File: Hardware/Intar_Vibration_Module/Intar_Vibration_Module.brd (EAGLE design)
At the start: 17.8 x 25.9 mm, 14 parts, among them J2 GROVE-4P-2.0-3470130P1, M1 MOTORVIBE_COIN_SMD, Q1 MMBT2222A

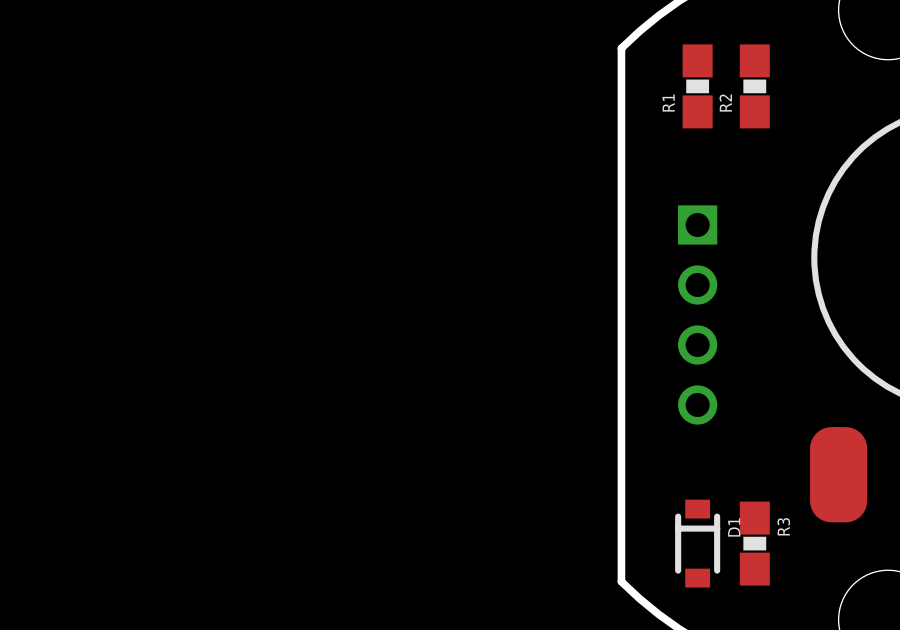
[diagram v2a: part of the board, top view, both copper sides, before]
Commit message: Fixed Grove connectors to be right way (pin 4 should be GND)
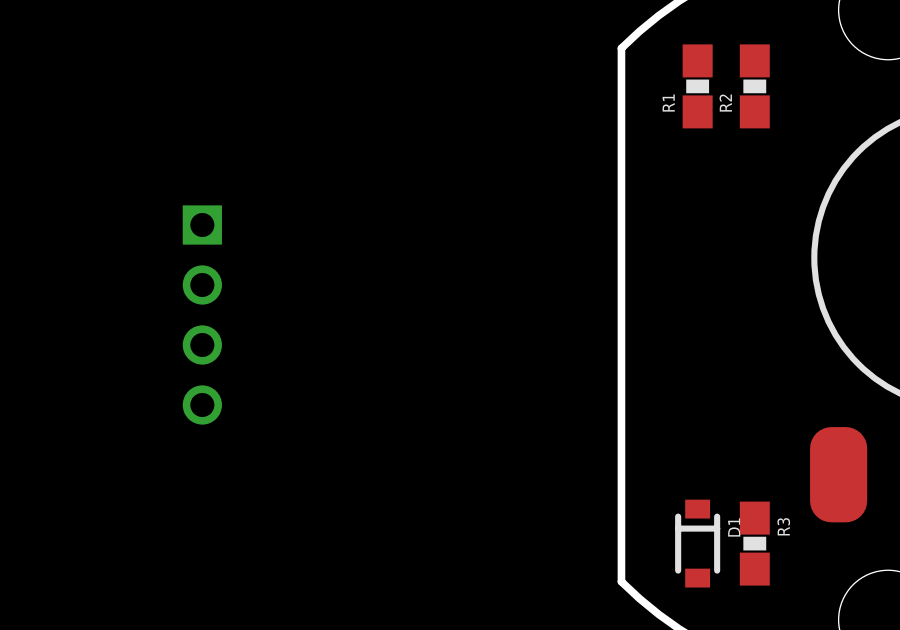
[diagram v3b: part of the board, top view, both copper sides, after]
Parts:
- removed J2: GROVE-4P-2.0-3470130P1, Connector:4P-2.0
- added J1: GROVE-4P-2.0-3470130P1, Connector:4P-2.0
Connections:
- net GND: now also J1.4; no longer J2.1
- net SIG: now also J1.1; no longer J2.4
- net VCC: now also J1.3; no longer J2.2
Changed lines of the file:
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@@
 <setting verticaltext="up"/>
 </settings>
-<grid distance="0.05" unitdist="inch" unit="inch" style="dots" multiple="1" display="yes" altdistance="0.025" altunitdist="inch" altunit="inch"/>
+<grid distance="0.05" unitdist="inch" unit="inch" style="dots" multiple="1" display="yes" altdistance="0.005" altunitdist="inch" altunit="inch"/>
 <layers>
 <layer number="1" name="Top" color="4" fill="1" visible="yes" active="yes"/>
 <layer number="2" name="Route2" color="1" fill="3" visible="no" active="yes"/>
 <layer number="15" name="Route15" color="4" fill="6" visible="no" active="yes"/>
-<layer number="16" name="Bottom" color="1" fill="1" visible="no" active="yes"/>
+<layer number="16" name="Bottom" color="1" fill="1" visible="yes" active="yes"/>
 <layer number="17" name="Pads" color="2" fill="1" visible="yes" active="yes"/>
 <layer number="18" name="Vias" color="2" fill="1" visible="yes" active="yes"/>
@@
 <layer number="20" name="Dimension" color="15" fill="1" visible="yes" active="yes"/>
 <layer number="21" name="tPlace" color="16" fill="1" visible="yes" active="yes"/>
-<layer number="22" name="bPlace" color="14" fill="1" visible="no" active="yes"/>
+<layer number="22" name="bPlace" color="14" fill="1" visible="yes" active="yes"/>
 <layer number="23" name="tOrigins" color="15" fill="1" visible="yes" active="yes"/>
-<layer number="24" name="bOrigins" color="15" fill="1" visible="no" active="yes"/>
+<layer number="24" name="bOrigins" color="15" fill="1" visible="yes" active="yes"/>
 <layer number="25" name="tNames" color="7" fill="1" visible="no" active="yes"/>
 <layer number="26" name="bNames" color="7" fill="1" visible="no" active="yes"/>
@@
 <layer number="43" name="vRestrict" color="2" fill="10" visible="no" active="yes"/>
 <layer number="44" name="Drills" color="7" fill="1" visible="no" active="yes"/>
-<layer number="45" name="Holes" color="7" fill="1" visible="no" active="yes"/>
+<layer number="45" name="Holes" color="7" fill="1" visible="yes" active="yes"/>
 <layer number="46" name="Milling" color="3" fill="1" visible="no" active="yes"/>
 <layer number="47" name="Measures" color="7" fill="1" visible="no" active="yes"/>
-<layer number="51" name="tDocu" color="6" fill="1" visible="no" active="yes"/>
+<layer number="51" name="tDocu" color="6" fill="1" visible="yes" active="yes"/>
 <layer number="52" name="bDocu" color="7" fill="1" visible="no" active="yes"/>
 <layer number="3" name="Route3" color="4" fill="3" visible="no" active="no"/>
@@
 <element name="FID2" library="SparkFun-Aesthetics" package="FIDUCIAL-1X2" value="FIDUCIAL1X2" x="-36.83" y="34.29"/>
 <element name="FRAME1" library="SparkFun-Aesthetics" package="CREATIVE_COMMONS" value="FRAME-LETTER" x="-101.6" y="16.51"/>
-<element name="J2" library="Connector" package="4P-2.0" value="GROVE-4P-2.0-3470130P1" x="-6.35" y="0" rot="MR270"/>
 <element name="LOGO1" library="SparkFun-Aesthetics" package="OSHW-LOGO-S" value="OSHW-LOGOS" x="-30.48" y="34.29"/>
 <element name="M1" library="Intar_Eagle_Library" package="VIBE_COIN_SMD" value="MOTORVIBE_COIN_SMD" x="2.54" y="1.905"/>
@@
 <element name="STANDOFF2" library="SparkFun-Electromechanical" package="STAND-OFF" value="STAND-OFF" x="0" y="-10.16"/>
 <element name="U$1" library="Intar_Eagle_Library" package="LOGO_SM" value="LOGOSM" x="-31.75" y="10.16"/>
+<element name="J1" library="Connector" package="4P-2.0" value="GROVE-4P-2.0-3470130P1" x="-22.86" y="0" rot="MR270"/>
 </elements>
 <signals>
 <signal name="GND">
-<contactref element="J2" pad="1"/>
 <contactref element="R2" pad="1"/>
 <contactref element="Q1" pad="2"/>
-<wire x1="-6.35" y1="3" x2="-4.445" y2="6.77" width="0" layer="19" extent="1-1"/>
-<wire x1="4.08" y1="7.94" x2="-6.35" y2="3" width="0" layer="19" extent="1-1"/>
+<contactref element="J1" pad="4"/>
+<wire x1="-4.445" y1="6.77" x2="-22.86" y2="-3" width="0" layer="19" extent="1-1"/>
+<wire x1="4.08" y1="7.94" x2="-4.445" y2="6.77" width="0" layer="19" extent="1-1"/>
 </signal>
 <signal name="VCC">
-<contactref element="J2" pad="2"/>
 <contactref element="D1" pad="C"/>
 <contactref element="M1" pad="1"/>
-<wire x1="-6.35" y1="1" x2="-6.35" y2="-6.47" width="0" layer="19" extent="1-1"/>
+<contactref element="J1" pad="3"/>
+<wire x1="-6.35" y1="-6.47" x2="-22.86" y2="-1" width="0" layer="19" extent="1-1"/>
 <wire x1="6.731" y1="-5.324" x2="-6.35" y2="-6.47" width="0" layer="19" extent="1-1"/>
 </signal>
 <signal name="SIG">
-<contactref element="J2" pad="4"/>
 <contactref element="R1" pad="1"/>
-<wire x1="-6.35" y1="-3" x2="-6.35" y2="6.77" width="0" layer="19" extent="1-1"/>
+<contactref element="J1" pad="1"/>
+<wire x1="-6.35" y1="6.77" x2="-22.86" y2="3" width="0" layer="19" extent="1-1"/>
 </signal>
 <signal name="N$2">

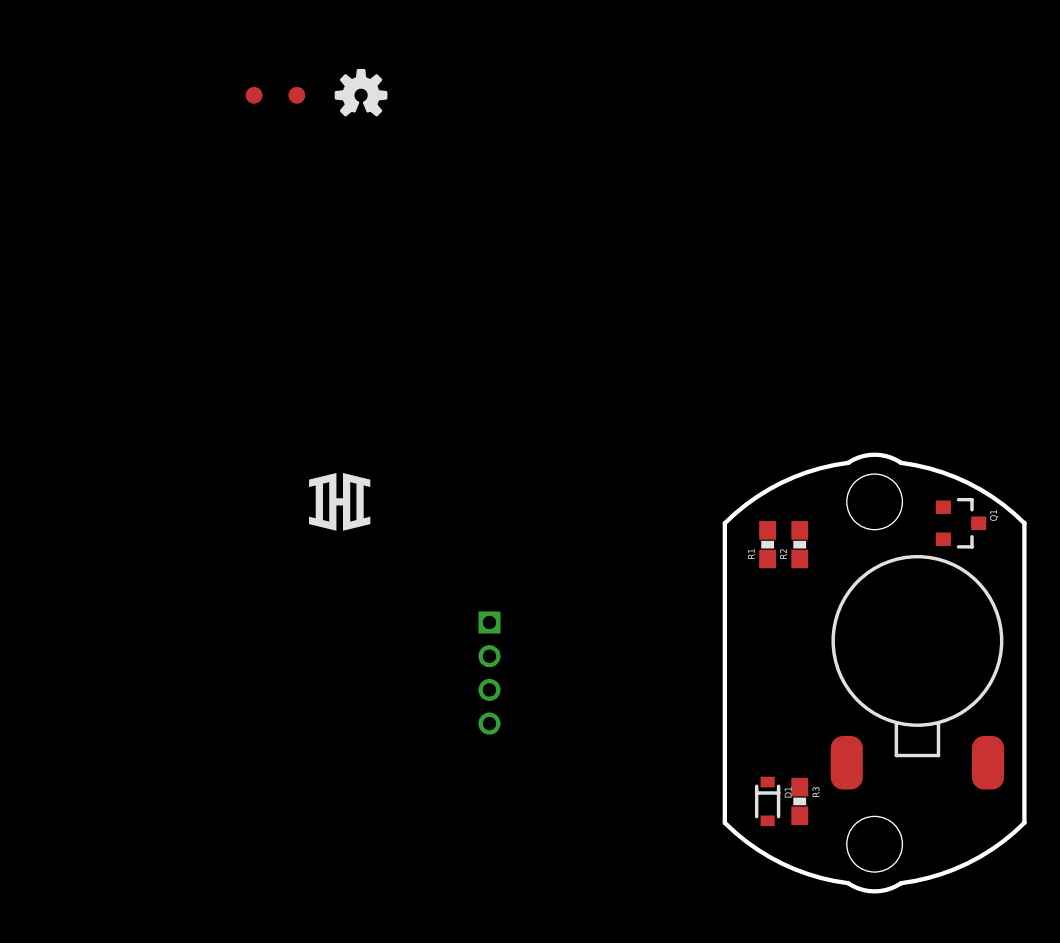
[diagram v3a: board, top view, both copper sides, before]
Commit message: Completed Vibration Module v01 layout
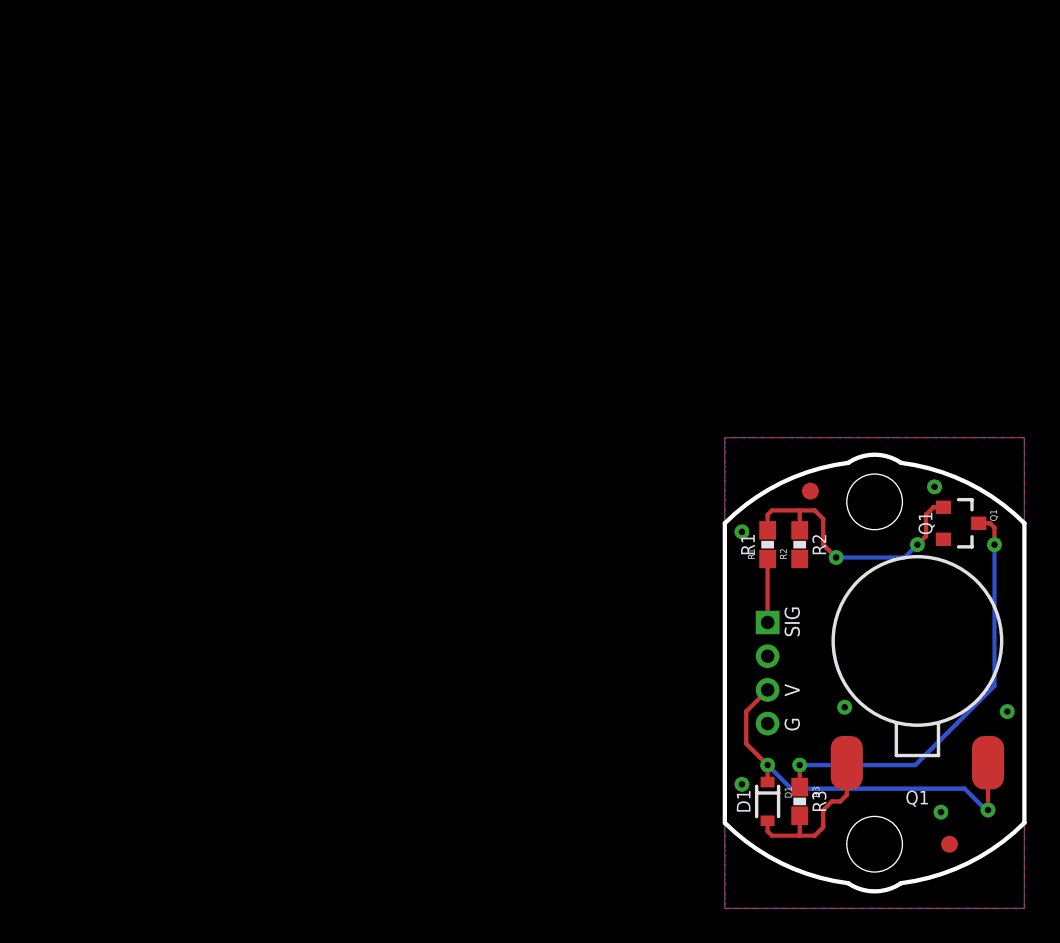
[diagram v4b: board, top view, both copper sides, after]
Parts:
- moved FRAME1 79.1 mm to (-33.0, -22.9)
- moved FID1 59.0 mm to (4.45, -10.2)
- moved LOGO1 43.6 mm to (4.45, 8.26), flipped to the bottom, turned to 270 degrees
- moved U$1 40.6 mm to (4.45, -8.26), flipped to the bottom, turned to 270 degrees
- moved FID2 40.5 mm to (-3.81, 10.8)
- moved J1 16.5 mm to (-6.35, 0.00)
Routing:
- net N$5: track 0.00 -> 25.2 mm, vias 0 -> 2
- net VCC: track 0.00 -> 23.5 mm, vias 0 -> 2
- net N$2: track 0.00 -> 16.7 mm, vias 0 -> 2
- net N$6: track 0.00 -> 10.1 mm
- net SIG: track 0.00 -> 3.77 mm
- added copper zone on layer 1, net GND
- added copper zone on layer 16, net GND
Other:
- board text added: "D1"
- board text added: "G"
- board text added: "Intar Vibration Module"
- board text added: "Q1"
- board text added: "R1"
- board text added: "R2"
- board text added: "R3"
- board text added: "SIG"
- board text added: "Shawn Hymel"
- board text added: "V"

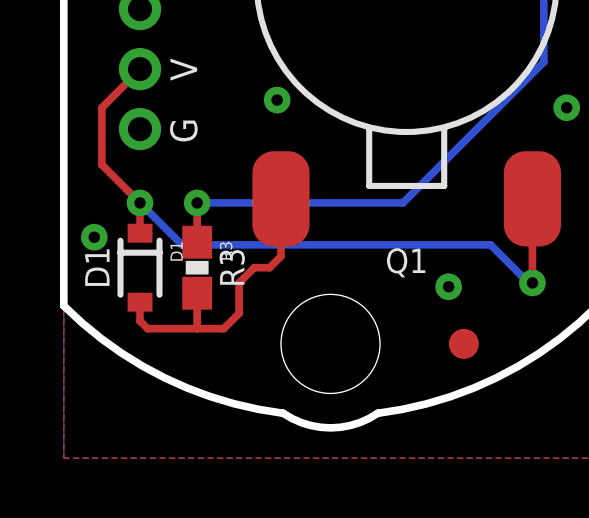
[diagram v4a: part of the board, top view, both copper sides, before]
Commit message: Moved IHI and OSH logos away from name on all boards.
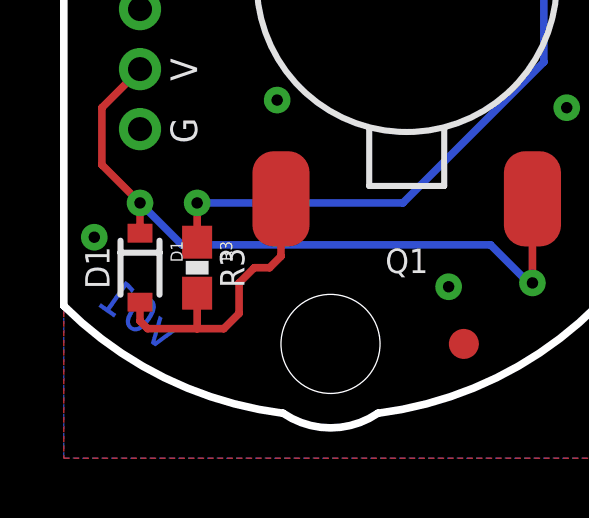
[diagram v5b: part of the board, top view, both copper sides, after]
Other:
- board text added: "v01"
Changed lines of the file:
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@@
 <setting verticaltext="up"/>
 </settings>
-<grid distance="0.01" unitdist="inch" unit="inch" style="dots" multiple="1" display="yes" altdistance="0.005" altunitdist="inch" altunit="inch"/>
+<grid distance="0.05" unitdist="inch" unit="inch" style="dots" multiple="1" display="yes" altdistance="0.005" altunitdist="inch" altunit="inch"/>
 <layers>
 <layer number="1" name="Top" color="4" fill="1" visible="yes" active="yes"/>
@@
 <layer number="45" name="Holes" color="7" fill="1" visible="yes" active="yes"/>
 <layer number="46" name="Milling" color="3" fill="1" visible="no" active="yes"/>
-<layer number="47" name="Measures" color="7" fill="1" visible="yes" active="yes"/>
+<layer number="47" name="Measures" color="7" fill="1" visible="no" active="yes"/>
 <layer number="51" name="tDocu" color="6" fill="1" visible="yes" active="yes"/>
 <layer number="52" name="bDocu" color="7" fill="1" visible="no" active="yes"/>
@@
 <text x="3.429" y="8.89" size="0.8128" layer="21" font="vector" ratio="15" rot="R270" align="top-center">Q1</text>
 <text x="2.54" y="-6.985" size="0.8128" layer="21" font="vector" ratio="15" align="top-center">Q1</text>
+<text x="-6.35" y="-9.144" size="1.2192" layer="16" font="vector" ratio="15" rot="SMR35" align="center">v01</text>
 </plain>
 <attributes>
